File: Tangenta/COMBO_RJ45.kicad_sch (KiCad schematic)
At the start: 1 part, among them J14 RC01133

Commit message: initialize branch
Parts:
- renumbered J14 to J17
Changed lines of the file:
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@@
   (symbol (lib_id "CholaSymbolsPrjLib:RC01133") (at 167.64 97.155 270) (unit 1)
     (in_bom yes) (on_board yes) (dnp no) (fields_autoplaced)
-    (property "Reference" "J14" (at 185.42 95.885 0)
+    (property "Reference" "J17" (at 185.42 95.885 0)
       (effects (font (size 1.27 1.27)))
     )
@@
     (instances
       (project "Tangenta"
-        (path "/358d1bcf-7599-4352-8c4d-baa18a5f09e6/98e3b24f-9927-4339-b8fd-9deea91a522a"
-          (reference "J14") (unit 1)
-        )
         (path "/358d1bcf-7599-4352-8c4d-baa18a5f09e6/da6cda23-cac5-483b-bd71-d8f2b2c13669"
           (reference "J17") (unit 1)

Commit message: J17,U24-26
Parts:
- J17: footprint RJ45_SIMPLE:RJ45_SIMPLE -> CholaFootprintsPrjLib:RJ45_SIMPLE
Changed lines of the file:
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@@
       (effects (font (size 1.27 1.27)))
     )
-    (property "Footprint" "RJ45_SIMPLE:RJ45_SIMPLE" (at 142.24 98.425 0)
+    (property "Footprint" "CholaFootprintsPrjLib:RJ45_SIMPLE" (at 142.24 98.425 0)
       (effects (font (size 1.27 1.27) italic) hide)
     )

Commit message: Removing component association with previous project (local) libraries.
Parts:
- J17: footprint CholaFootprintsPrjLib:RJ45_SIMPLE -> RJ45_SIMPLE:RJ45_SIMPLE; symbol CholaSymbolsPrjLib:RC01133 -> RC01133:RC01133
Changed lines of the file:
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@@
 	)
 	(symbol
-		(lib_id "CholaSymbolsPrjLib:RC01133")
+		(lib_id "RC01133:RC01133")
 		(at 167.64 97.155 270)
 		(unit 1)
@@
 			)
 		)
-		(property "Footprint" "CholaFootprintsPrjLib:RJ45_SIMPLE"
+		(property "Footprint" "RJ45_SIMPLE:RJ45_SIMPLE"
 			(at 142.24 98.425 0)
 			(effects

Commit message: Fixes, before checks.
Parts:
- J17: symbol RC01133:RC01133 -> RJ45_SIMPLE:RC01133
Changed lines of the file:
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@@
 	)
 	(symbol
-		(lib_id "RC01133:RC01133")
+		(lib_id "RJ45_SIMPLE:RC01133")
 		(at 167.64 97.155 270)
 		(unit 1)

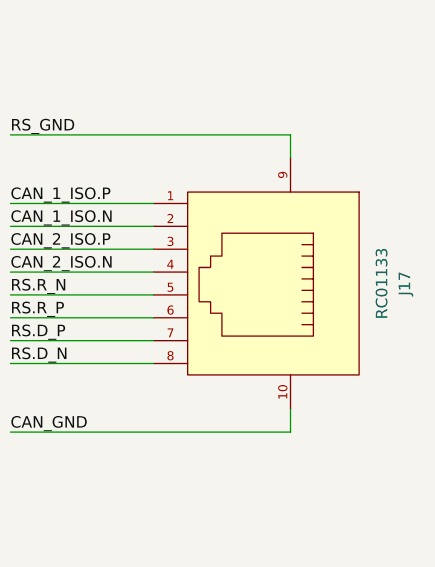
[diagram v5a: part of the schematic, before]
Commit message: Reverting to the original design.
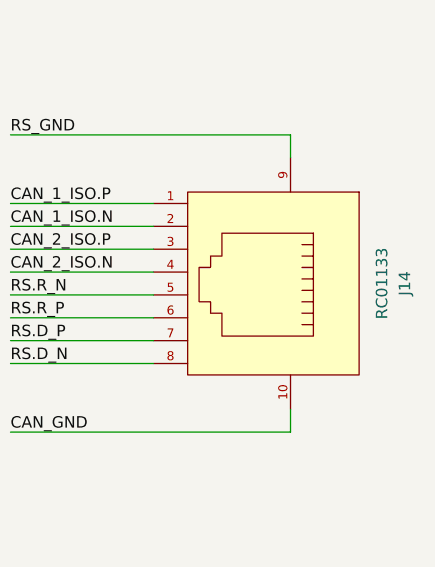
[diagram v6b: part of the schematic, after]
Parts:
- J14: renamed from J17; symbol RJ45_SIMPLE:RC01133 -> CholaSymbolsPrjLib:RC01133

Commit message: ...
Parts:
- J14: symbol CholaSymbolsPrjLib:RC01133 -> LocalPrjLib:RC01133
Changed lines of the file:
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@@
     (effects (font (size 1.27 1.27)) (justify right))
   )
-  (symbol (lib_id "CholaSymbolsPrjLib:RC01133") (at 167.64 97.155 270) (unit 1)
+  (symbol (lib_id "LocalPrjLib:RC01133") (at 167.64 97.155 270) (unit 1)
     (in_bom yes) (on_board yes) (dnp no) (fields_autoplaced)
     (property "Reference" "J14" (at 185.42 95.885 0)

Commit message: Fixes, new approach.
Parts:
- J14: symbol LocalPrjLib:RC01133 -> LocalSymbolsPrjLib:RC01133
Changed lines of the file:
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@@
     (effects (font (size 1.27 1.27)) (justify right))
   )
-  (symbol (lib_id "LocalPrjLib:RC01133") (at 167.64 97.155 270) (unit 1)
+  (symbol (lib_id "LocalSymbolsPrjLib:RC01133") (at 167.64 97.155 270) (unit 1)
     (in_bom yes) (on_board yes) (dnp no) (fields_autoplaced)
     (property "Reference" "J14" (at 185.42 95.885 0)
